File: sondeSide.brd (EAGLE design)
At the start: 105.2 x 31.8 mm, 41 parts

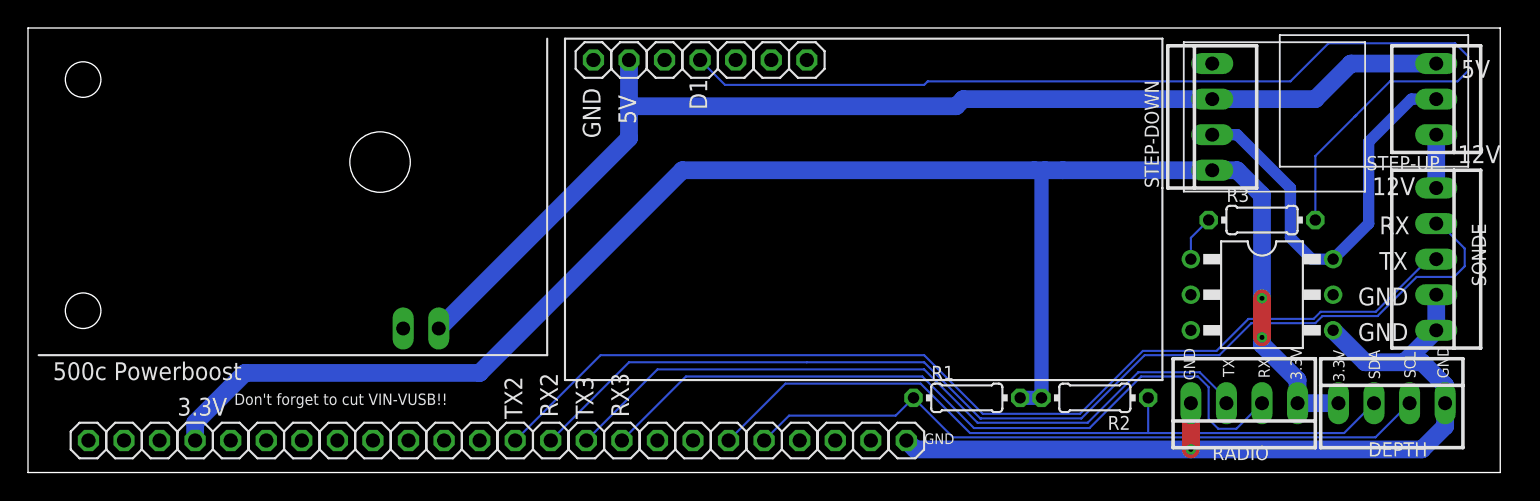
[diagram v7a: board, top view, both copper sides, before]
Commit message: Last push before switching to live-switch SSR
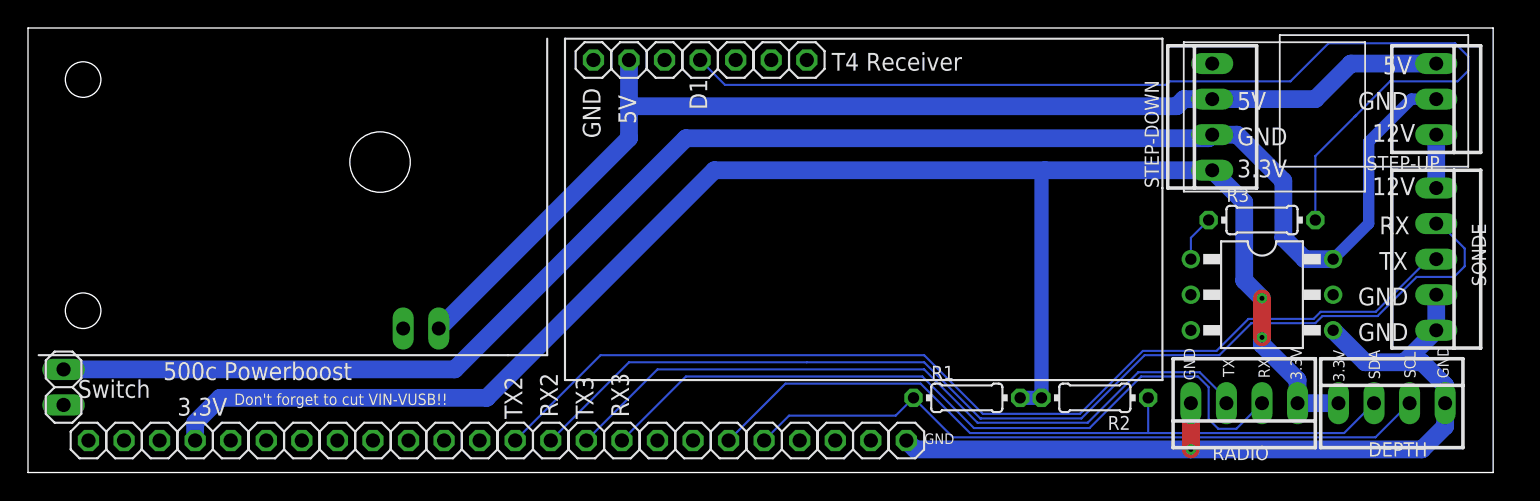
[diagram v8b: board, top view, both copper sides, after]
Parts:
- added JP25: (no value), pinhead:1X02
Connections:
- net GND: now also JP25.1
- net GND_PLANE: now also JP25.2
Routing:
- net GND: track 91.5 -> 181.7 mm
- net 3.3V: track 125.9 -> 124.9 mm
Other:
- board size 105.2 x 31.8 mm -> 104.6 x 31.8 mm
- board text added: "Switch"
- board text added: "T4 Receiver"
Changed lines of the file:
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@@
 <board>
 <plain>
-<wire x1="0" y1="0" x2="105.156" y2="0" width="0" layer="20"/>
-<wire x1="105.156" y1="0" x2="105.156" y2="31.75" width="0" layer="20"/>
-<wire x1="105.156" y1="31.75" x2="0" y2="31.75" width="0" layer="20"/>
+<wire x1="0" y1="0" x2="104.648" y2="0" width="0" layer="20"/>
+<wire x1="104.648" y1="0" x2="104.648" y2="31.75" width="0" layer="20"/>
+<wire x1="104.648" y1="31.75" x2="0" y2="31.75" width="0" layer="20"/>
 <wire x1="0" y1="31.75" x2="0" y2="0" width="0" layer="20"/>
 <text x="101.473" y="6.731" size="0.8128" layer="25" rot="R90">GND</text>
@@
 <text x="41.402" y="28.956" size="1.27" layer="26" rot="MR270">RX3</text>
 <text x="41.656" y="7.112" size="1.27" layer="25" rot="R270">RX3</text>
-<text x="102.362" y="28.194" size="1.27" layer="25">5V</text>
+<text x="96.774" y="28.448" size="1.27" layer="25">5V</text>
 <text x="58.166" y="22.86" size="1.27" layer="26" rot="MR270">5V</text>
 <text x="60.96" y="22.86" size="1.27" layer="26" rot="MR270">GND</text>
 <text x="64.008" y="2.032" size="0.762" layer="25">GND</text>
-<text x="102.108" y="22.098" size="1.27" layer="25">12V</text>
+<text x="96.012" y="23.622" size="1.27" layer="25">12V</text>
 <text x="63.5" y="22.86" size="1.27" layer="26" rot="MR270">12V</text>
 <text x="14.732" y="4.826" size="0.8128" layer="25">Don't forget to cut VIN-VUSB!!</text>
@@
 <hole x="25.146" y="22.1742" drill="4.318"/>
 <hole x="3.937" y="28.067" drill="2.54"/>
-<text x="1.778" y="6.604" size="1.27" layer="25">500c Powerboost</text>
+<text x="9.652" y="6.604" size="1.27" layer="25">500c Powerboost</text>
 <wire x1="0.762" y1="8.382" x2="34.29" y2="8.382" width="0.1524" layer="21"/>
 <wire x1="34.29" y1="8.382" x2="37.084" y2="8.382" width="0.1524" layer="21"/>
 <wire x1="37.084" y1="8.382" x2="37.084" y2="30.988" width="0.1524" layer="21"/>
-<rectangle x1="-15.748" y1="35.052" x2="4.572" y2="85.852" layer="114" rot="R90"/>
 <wire x1="38.354" y1="30.988" x2="81.026" y2="30.988" width="0.1524" layer="21"/>
 <wire x1="81.026" y1="30.988" x2="81.026" y2="20.32" width="0.1524" layer="21"/>
@@
 <text x="43.434" y="24.892" size="1.27" layer="25" rot="R90">5V</text>
 <text x="48.514" y="25.908" size="1.27" layer="25" rot="R90">D1</text>
+<text x="3.556" y="5.334" size="1.27" layer="21">Switch</text>
+<text x="86.36" y="25.908" size="1.27" layer="25">5V</text>
+<text x="86.36" y="21.082" size="1.27" layer="25">3.3V</text>
+<text x="94.996" y="25.908" size="1.27" layer="25">GND</text>
+<text x="86.36" y="23.368" size="1.27" layer="25">GND</text>
+<text x="57.404" y="28.702" size="1.27" layer="25">T4 Receiver</text>
 </plain>
 <attributes>
@@
 <attribute name="SPICEPREFIX" value="R" x="88.138" y="18.034" size="1.778" layer="27" display="off"/>
 </element>
+<element name="JP25" library="pinhead" library_urn="urn:adsk.eagle:library:325" package="1X02" package3d_urn="urn:adsk.eagle:package:22435/2" value="" x="2.54" y="6.096" smashed="yes" rot="R270">
+<attribute name="VALUE" x="-0.635" y="8.636" size="1.27" layer="27" rot="R270"/>
+</element>
 </elements>
 <signals>
@@
 <wire x1="84.582" y1="21.59" x2="81.026" y2="21.59" width="0.8128" layer="16"/>
 <wire x1="11.938" y1="3.556" x2="11.938" y2="2.286" width="1.27" layer="16"/>
-<wire x1="84.582" y1="21.59" x2="73.914" y2="21.59" width="1.27" layer="16"/>
-<wire x1="73.914" y1="21.59" x2="72.644" y2="21.59" width="1.27" layer="16"/>
-<wire x1="72.644" y1="21.59" x2="71.882" y2="21.59" width="1.27" layer="16"/>
-<wire x1="71.882" y1="21.59" x2="46.736" y2="21.59" width="1.27" layer="16"/>
-<wire x1="46.736" y1="21.59" x2="32.258" y2="7.112" width="1.27" layer="16"/>
-<wire x1="32.258" y1="7.112" x2="15.494" y2="7.112" width="1.27" layer="16"/>
-<wire x1="15.494" y1="7.112" x2="11.938" y2="3.556" width="1.27" layer="16"/>
-<wire x1="84.582" y1="21.59" x2="86.36" y2="21.59" width="1.27" layer="16"/>
+<wire x1="84.582" y1="21.59" x2="72.644" y2="21.59" width="1.27" layer="16"/>
+<wire x1="72.644" y1="21.59" x2="49.022" y2="21.59" width="1.27" layer="16"/>
+<wire x1="49.022" y1="21.59" x2="32.766" y2="5.334" width="1.27" layer="16"/>
+<wire x1="32.766" y1="5.334" x2="13.716" y2="5.334" width="1.27" layer="16"/>
+<wire x1="13.716" y1="5.334" x2="11.938" y2="3.556" width="1.27" layer="16"/>
 <wire x1="90.678" y1="6.604" x2="90.678" y2="4.953" width="1.27" layer="16"/>
-<wire x1="86.36" y1="21.59" x2="88.138" y2="19.812" width="1.27" layer="16"/>
-<wire x1="88.138" y1="19.812" x2="88.138" y2="12.446" width="1.27" layer="16"/>
 <wire x1="88.138" y1="9.652" x2="88.138" y2="9.144" width="1.27" layer="16"/>
 <wire x1="88.138" y1="9.144" x2="90.678" y2="6.604" width="1.27" layer="16"/>
@@
 <wire x1="72.39" y1="5.334" x2="72.39" y2="21.336" width="1.016" layer="16"/>
 <wire x1="72.39" y1="21.336" x2="72.644" y2="21.59" width="1.016" layer="16"/>
+<wire x1="84.582" y1="21.59" x2="86.868" y2="19.304" width="1.27" layer="16"/>
+<wire x1="86.868" y1="13.716" x2="88.138" y2="12.446" width="1.27" layer="16"/>
+<wire x1="86.868" y1="19.304" x2="86.868" y2="13.716" width="1.27" layer="16"/>
 </signal>
 <signal name="GND">
@@
 <wire x1="98.298" y1="7.874" x2="95.504" y2="7.874" width="1.27" layer="16"/>
 <wire x1="95.504" y1="7.874" x2="93.218" y2="10.16" width="1.27" layer="16"/>
-<wire x1="84.582" y1="24.13" x2="86.36" y2="24.13" width="0.8128" layer="16"/>
-<wire x1="86.36" y1="24.13" x2="90.17" y2="20.32" width="0.8128" layer="16"/>
-<wire x1="91.694" y1="15.24" x2="93.218" y2="15.24" width="0.8128" layer="16"/>
-<wire x1="90.17" y1="20.32" x2="90.17" y2="16.764" width="0.8128" layer="16"/>
-<wire x1="90.17" y1="16.764" x2="91.694" y2="15.24" width="0.8128" layer="16"/>
 <wire x1="100.584" y1="26.67" x2="98.806" y2="26.67" width="0.8128" layer="16"/>
 <wire x1="98.806" y1="26.67" x2="95.758" y2="23.622" width="0.8128" layer="16"/>
@@
 <wire x1="100.584" y1="10.16" x2="98.298" y2="7.874" width="1.27" layer="16"/>
 <wire x1="100.584" y1="10.16" x2="100.584" y2="12.7" width="1.27" layer="16"/>
-<wire x1="93.218" y1="10.16" x2="93.218" y2="15.24" width="0" layer="19" extent="1-1"/>
+<wire x1="84.582" y1="24.13" x2="86.36" y2="24.13" width="1.27" layer="16"/>
+<wire x1="91.186" y1="15.24" x2="93.218" y2="15.24" width="1.27" layer="16"/>
+<wire x1="86.36" y1="24.13" x2="89.662" y2="20.828" width="1.27" layer="16"/>
+<wire x1="89.662" y1="20.828" x2="89.662" y2="16.764" width="1.27" layer="16"/>
+<wire x1="89.662" y1="16.764" x2="91.186" y2="15.24" width="1.27" layer="16"/>
+<wire x1="84.582" y1="24.13" x2="84.328" y2="23.876" width="1.27" layer="16"/>
+<wire x1="84.328" y1="23.876" x2="46.99" y2="23.876" width="1.27" layer="16"/>
+<wire x1="46.99" y1="23.876" x2="30.48" y2="7.366" width="1.27" layer="16"/>
+<wire x1="30.48" y1="7.366" x2="2.54" y2="7.366" width="1.27" layer="16"/>
+<wire x1="3.429" y1="7.366" x2="2.54" y2="7.366" width="1.27" layer="16"/>
+<contactref element="JP25" pad="1"/>
+<wire x1="93.218" y1="15.24" x2="93.218" y2="10.16" width="0" layer="19" extent="1-1"/>
 </signal>
 <signal name="12V">
@@
 <wire x1="84.582" y1="26.67" x2="91.948" y2="26.67" width="1.27" layer="16"/>
 <wire x1="91.948" y1="26.67" x2="94.488" y2="29.21" width="1.27" layer="16"/>
-<wire x1="42.926" y1="26.162" x2="66.294" y2="26.162" width="1.27" layer="16"/>
-<wire x1="66.294" y1="26.162" x2="66.802" y2="26.67" width="1.27" layer="16"/>
-<wire x1="66.802" y1="26.67" x2="84.582" y2="26.67" width="1.27" layer="16"/>
+<wire x1="42.926" y1="26.162" x2="82.042" y2="26.162" width="1.27" layer="16"/>
+<wire x1="82.042" y1="26.162" x2="82.55" y2="26.67" width="1.27" layer="16"/>
+<wire x1="82.55" y1="26.67" x2="84.582" y2="26.67" width="1.27" layer="16"/>
 <wire x1="42.926" y1="26.162" x2="42.926" y2="26.416" width="0" layer="19" extent="16-16"/>
 </signal>
@@
 <contactref element="JP29" pad="1"/>
 <wire x1="48.006" y1="29.464" x2="49.784" y2="27.686" width="0.1524" layer="16"/>
-<wire x1="64.008" y1="27.686" x2="64.262" y2="27.94" width="0.1524" layer="16"/>
+<wire x1="81.28" y1="27.686" x2="81.534" y2="27.94" width="0.1524" layer="16"/>
 <wire x1="90.17" y1="27.94" x2="92.8878" y2="30.6578" width="0.1524" layer="16"/>
 <wire x1="101.9302" y1="30.6578" x2="102.87" y2="29.718" width="0.1524" layer="16"/>
 <wire x1="102.87" y1="29.718" x2="102.87" y2="28.702" width="0.1524" layer="16"/>
 <wire x1="102.87" y1="28.702" x2="102.108" y2="27.94" width="0.1524" layer="16"/>
-<wire x1="49.784" y1="27.686" x2="64.008" y2="27.686" width="0.1524" layer="16"/>
-<wire x1="64.262" y1="27.94" x2="90.17" y2="27.94" width="0.1524" layer="16"/>
+<wire x1="49.784" y1="27.686" x2="81.28" y2="27.686" width="0.1524" layer="16"/>
+<wire x1="81.534" y1="27.94" x2="90.17" y2="27.94" width="0.1524" layer="16"/>
 <wire x1="92.8878" y1="30.6578" x2="101.9302" y2="30.6578" width="0.1524" layer="16"/>
 <wire x1="102.108" y1="27.94" x2="97.282" y2="27.94" width="0.1524" layer="16"/>
@@
 <contactref element="JP26" pad="1"/>
 <contactref element="PWRBOOST" pad="1"/>
+<contactref element="JP25" pad="2"/>
 <wire x1="83.058" y1="12.7" x2="93.218" y2="12.7" width="0" layer="19" extent="1-1"/>
 <wire x1="40.386" y1="29.464" x2="83.058" y2="12.7" width="0" layer="19" extent="1-1"/>
 <wire x1="26.797" y1="10.287" x2="40.386" y2="29.464" width="0" layer="19" extent="1-1"/>
+<wire x1="2.54" y1="4.826" x2="26.797" y2="10.287" width="0" layer="19" extent="1-1"/>
 </signal>
 <signal name="D0">
